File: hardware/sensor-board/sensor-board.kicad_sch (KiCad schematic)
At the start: 27 parts

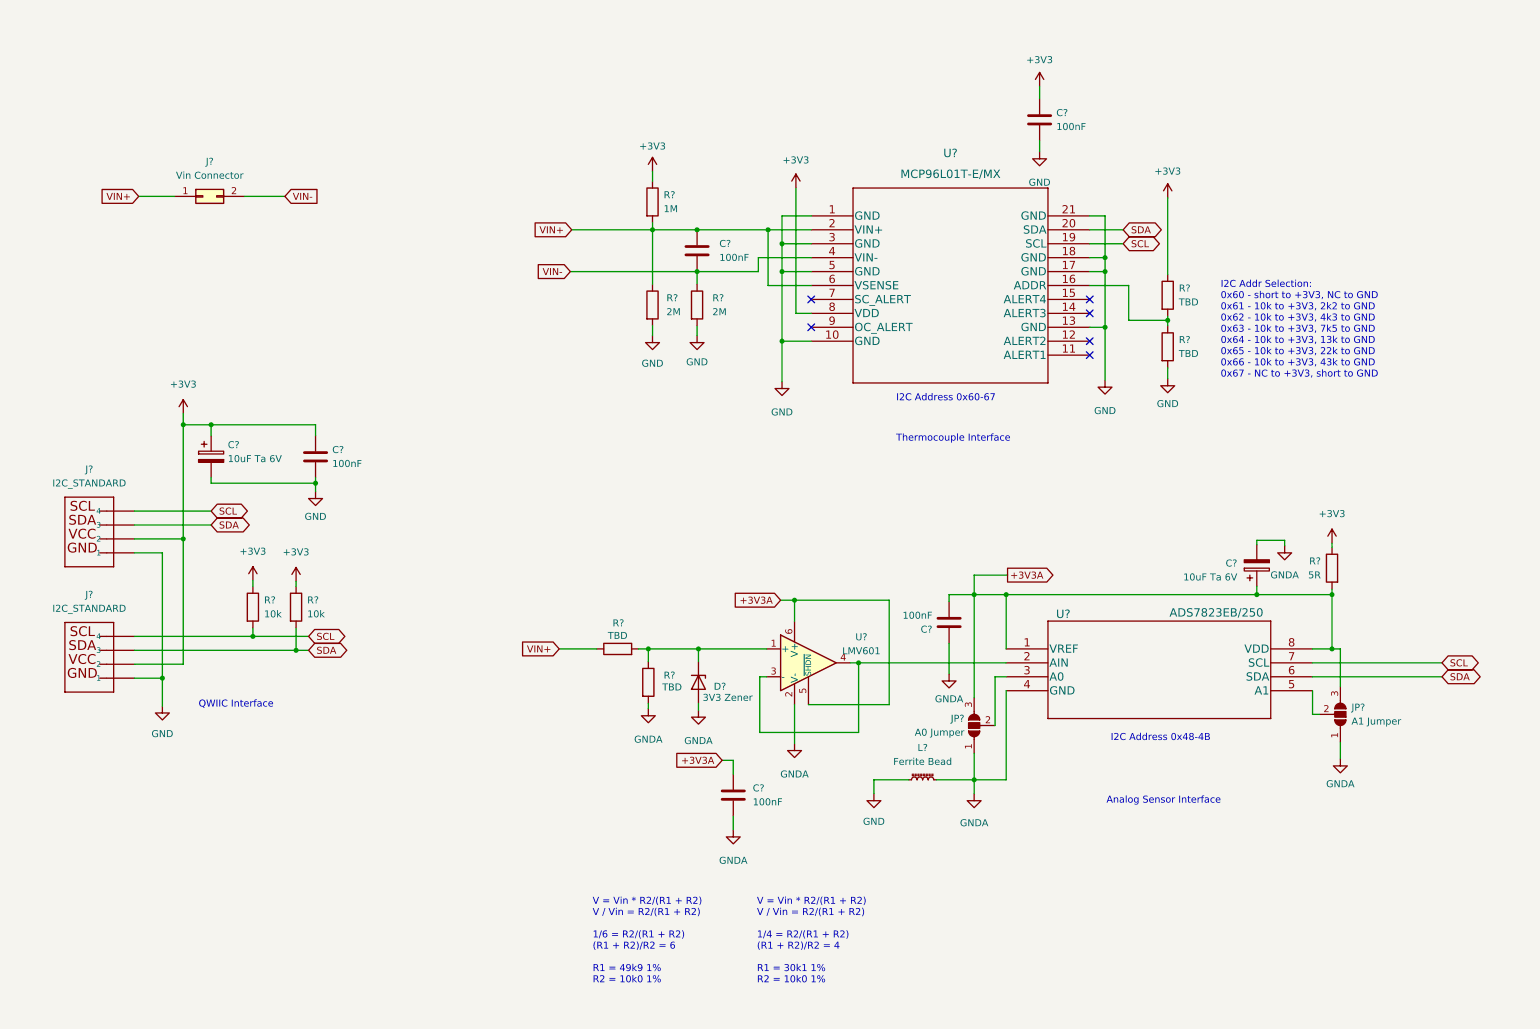
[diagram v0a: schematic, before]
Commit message: Added 1Wire sensor (over I2C) for outside temp
- coded up the first AnalogSourceBase and DS2482Source classes
- still need for ADC, thermocouple if... and internal temperature via
  internal ADC
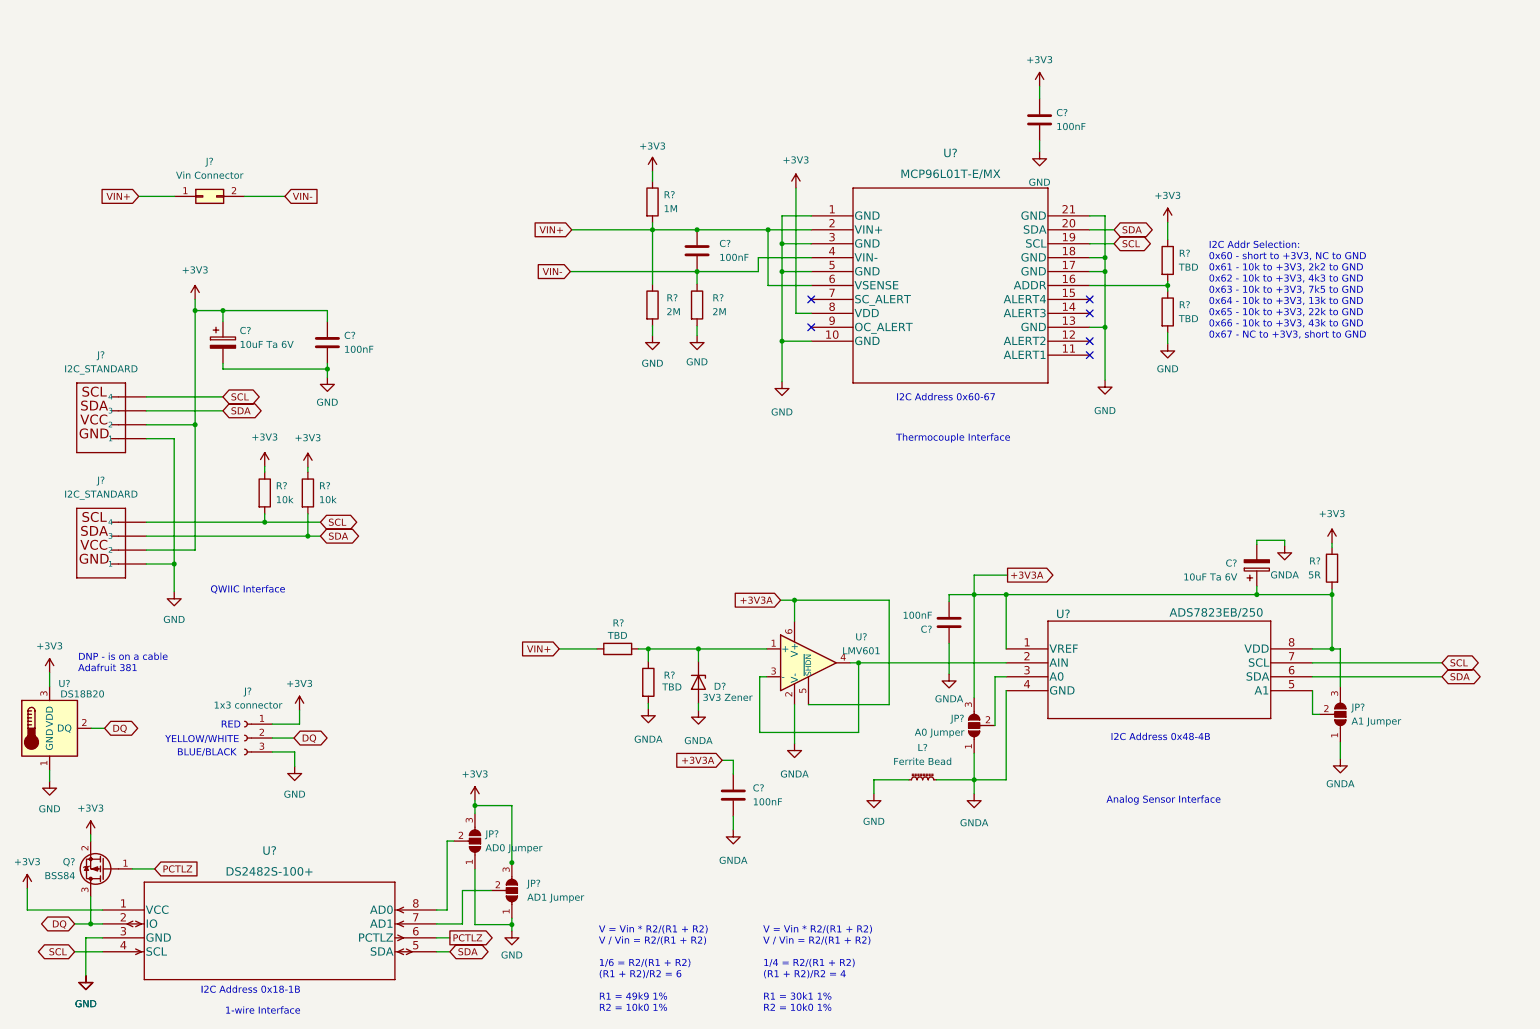
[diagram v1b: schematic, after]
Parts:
- added J?: 1x3 connector, symbol Connector:Conn_01x03_Female
- added JP?: AD1 Jumper, symbol Jumper:SolderJumper_3_Open
- added JP?: AD0 Jumper, symbol Jumper:SolderJumper_3_Open
- added Q?: BSS84, Package_TO_SOT_SMD:SOT-23, symbol Transistor_FET:BSS84
- added U?: DS18B20, Package_TO_SOT_THT:TO-92_Inline, symbol Sensor_Temperature:DS18B20
- added U?: DS2482S-100+, UltraLibrarian:ds2482s-100&plus_, symbol UltraLibrarian:DS2482S-100+
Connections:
- net +3V3: now also J?.1 (Pin_1), JP?.3 (B), JP?.3 (B), Q?.2 (S), U?.1 (VCC), U?.3 (VDD)
- net GND: now also J?.3 (Pin_3), JP?.1 (A), JP?.1 (A), U?.1 (GND), U?.3 (GND)
- net SCL: now also U?.4 (SCL)
- net SDA: now also U?.5 (SDA)
- new net: JP?.2 (C), U?.7 (AD1)
- new net: JP?.2 (C), U?.8 (AD0)
- new net DQ: J?.2 (Pin_2), Q?.3 (D), U?.2 (DQ), U?.2 (IO)
- new net PCTLZ: Q?.1 (G), U?.6 (PCTLZ)
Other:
- note added: "1-wire Interface"
- note added: "BLUE/BLACK"
- note added: "DNP - is on a cable Adafruit 381"
- note added: "I2C Address 0x18-1B"
- note added: "RED"
- note added: "YELLOW/WHITE"
- moved on the sheet: C?, J?, R?

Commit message: Layout v1 for sensors board
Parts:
- removed C? (x2): 10uF Ta 6V, symbol Device:C_Polarized
- added C1, C7: 10uF Ta 6V3, Capacitor_Tantalum_SMD:CP_EIA-3216-10_Kemet-I_Pad1.58x1.35mm_HandSolder, symbol Device:C_Polarized
- C2, C3, C4, C5, C6: renamed from C?; footprint (none) -> Capacitor_SMD:C_0805_2012Metric_Pad1.18x1.45mm_HandSolder
- D1: renamed from D?; value 3V3 Zener -> BZT52C3V3-7-F; footprint (none) -> Diode_SMD:D_SOD-123
- J1, J2: renamed from J?; value I2C_STANDARD -> QWIIC Connector; footprint UltraLibrarian:PRT-16766 -> Beirdo:QWIIC Connector
- J3: renamed from J?; footprint (none) -> TerminalBlock:TerminalBlock_Altech_AK300-2_P5.00mm
- J4: renamed from J?; footprint (none) -> TerminalBlock:TerminalBlock_Altech_AK300-3_P5.00mm
- JP1, JP2, JP3, JP4: renamed from JP?; footprint (none) -> Jumper:SolderJumper-3_P1.3mm_Open_Pad1.0x1.5mm
- L1: renamed from L?; footprint (none) -> Inductor_SMD:L_0805_2012Metric_Pad1.05x1.20mm_HandSolder
- R1, R10, R2, R3, R4, R5, R6, R7, R8, R9: renamed from R?; footprint (none) -> Resistor_SMD:R_0805_2012Metric_Pad1.20x1.40mm_HandSolder
- gave numbers to parts that had none: 6
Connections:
- net +3V3: now also C1.1
- net +3V3A: now also C5.1, JP3.3 (B), JP4.3 (B), R10.2, U5.1 (VREF), U5.8 (VDD), C7.1
- net GND: now also C1.2
- net GNDA: now also C7.2
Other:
- note added: "3.3V Zener"
- moved on the sheet: D1, R3, R4

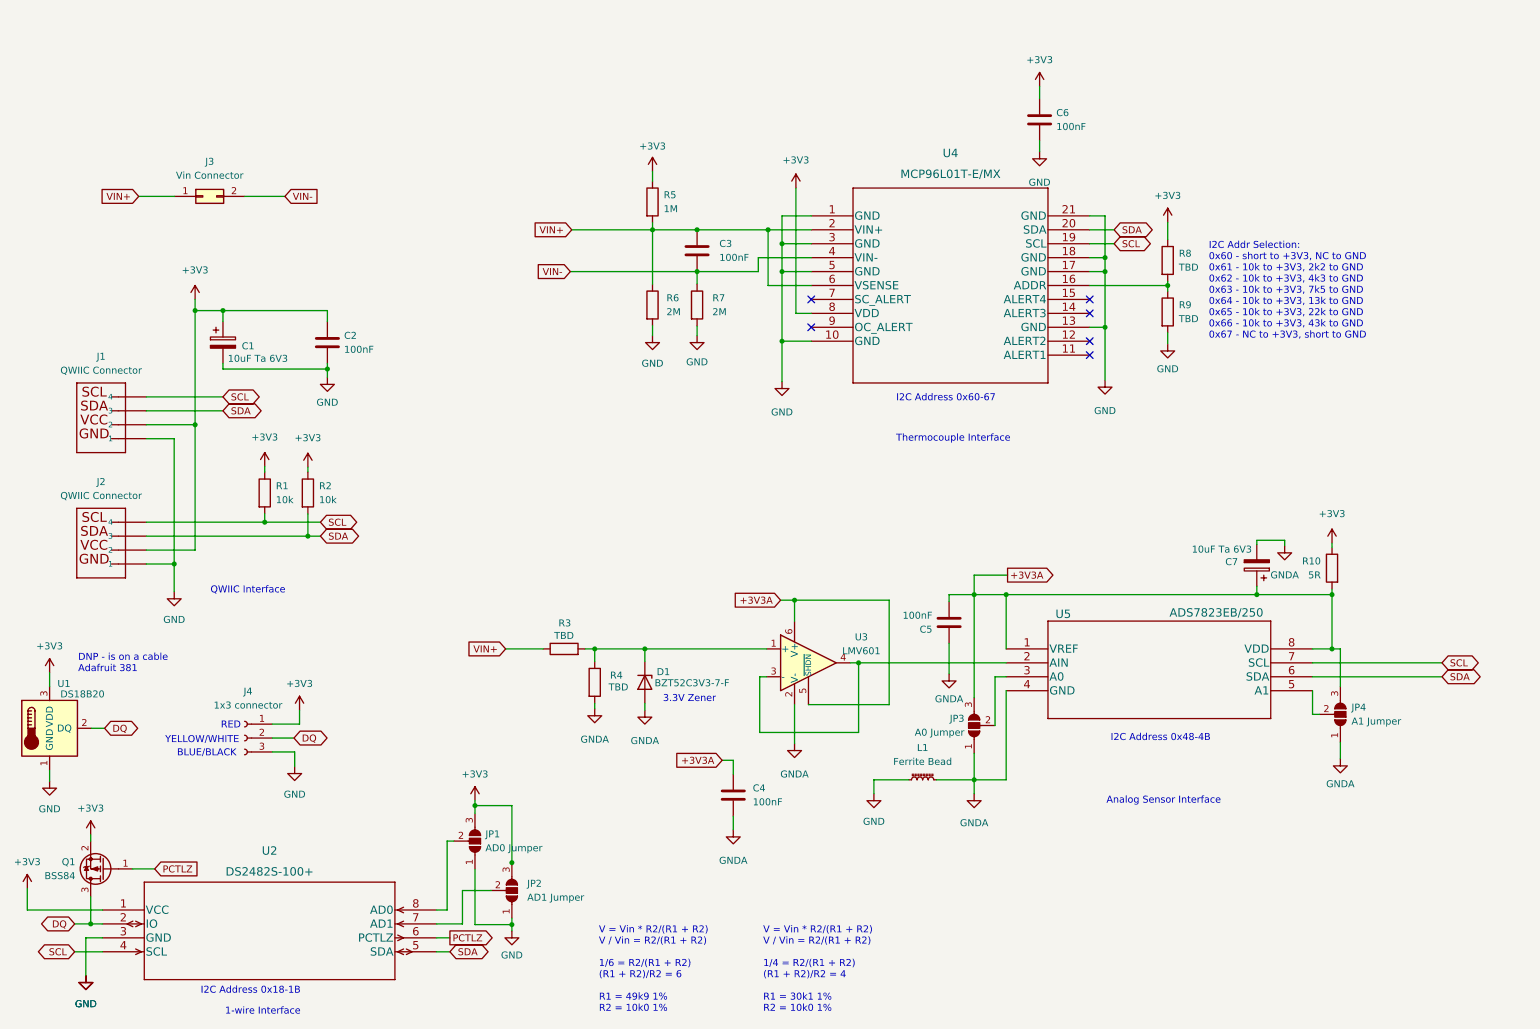
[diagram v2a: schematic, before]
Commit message: Added GPIO/EEPROM on sensor board
- this will allow me to connect the ignition wire, and also to have the
  boards report their capabilities to the firmware
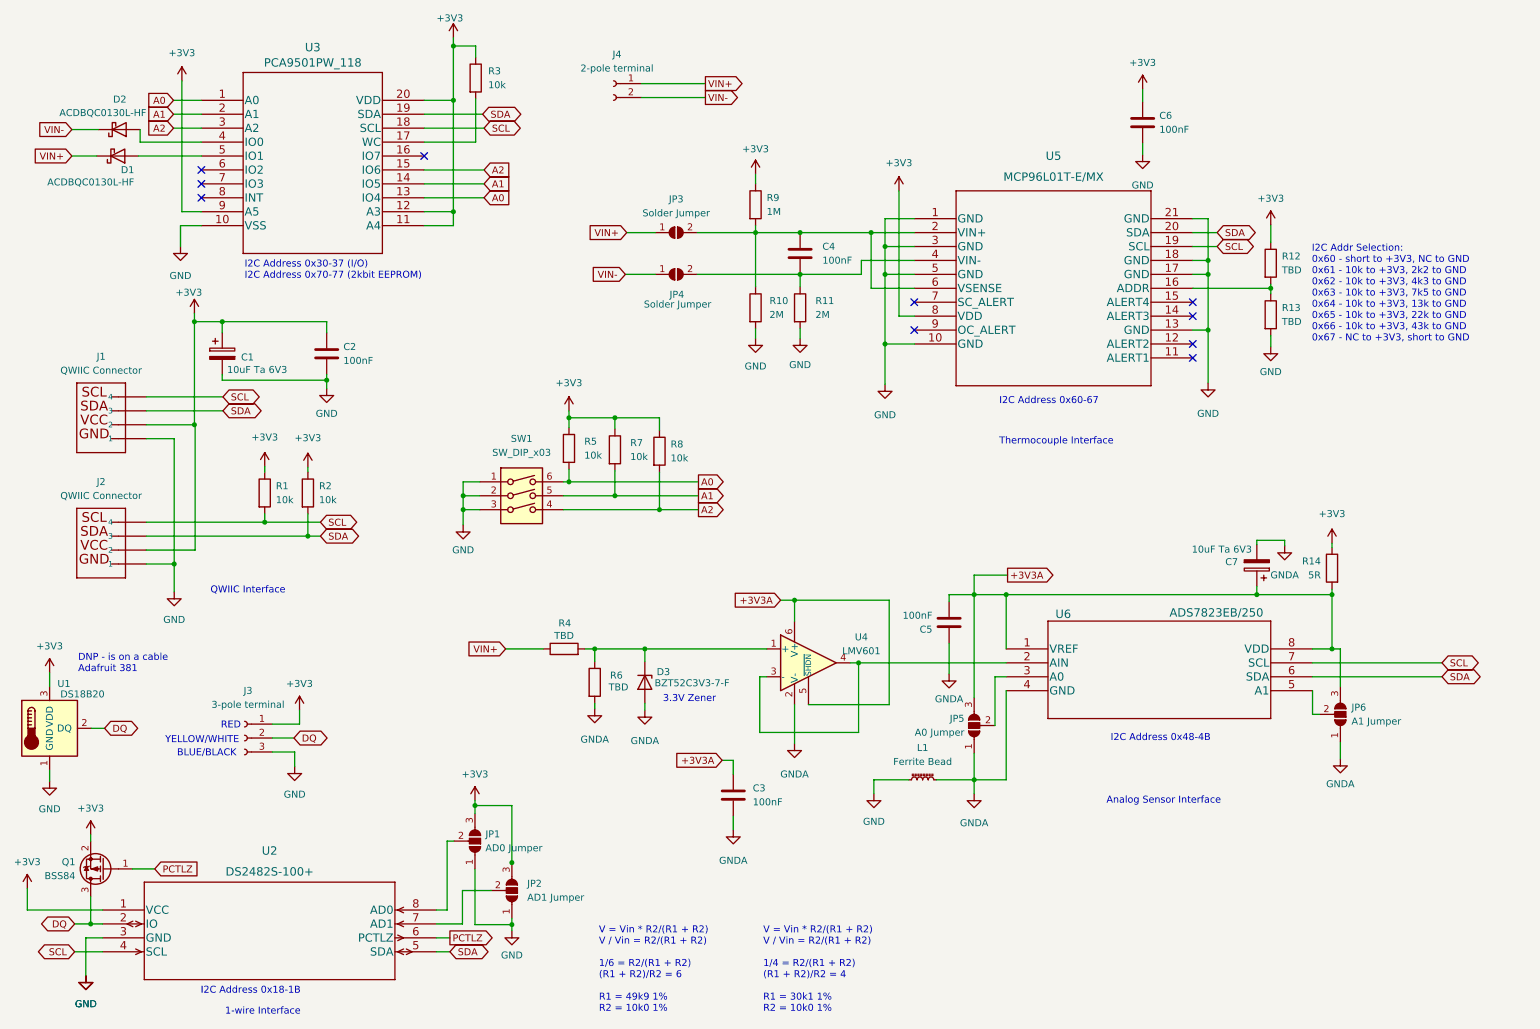
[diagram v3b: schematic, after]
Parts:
- removed J3: Vin Connector, TerminalBlock:TerminalBlock_Altech_AK300-2_P5.00mm, symbol Connector_Generic:Conn_02x01
- added D1, D2: ACDBQC0130L-HF, Diode_SMD:D_SOD-923, symbol Device:D_Schottky
- added J4: 2-pole terminal, TerminalBlock:TerminalBlock_Altech_AK300-2_P5.00mm, symbol Connector:Conn_01x02_Female
- added JP3, JP4: Solder Jumper, Jumper:SolderJumper-2_P1.3mm_Open_RoundedPad1.0x1.5mm, symbol Jumper:SolderJumper_2_Open
- added R3, R5, R7, R8: 10k, Resistor_SMD:R_0805_2012Metric_Pad1.20x1.40mm_HandSolder, symbol Device:R
- added SW1: SW_DIP_x03, Button_Switch_SMD:SW_DIP_SPSTx03_Slide_9.78x9.8mm_W8.61mm_P2.54mm, symbol Switch:SW_DIP_x03
- added U3: PCA9501PW_118, UltraLibrarian:PCA9501PW_118, symbol UltraLibrarian:PCA9501PW_118
- J3: renamed from J4; value 1x3 connector -> 3-pole terminal
- JP1, JP2: footprint Jumper:SolderJumper-3_P1.3mm_Open_Pad1.0x1.5mm -> Jumper:SolderJumper-3_P1.3mm_Open_RoundedPad1.0x1.5mm
- JP5: renamed from JP3; footprint Jumper:SolderJumper-3_P1.3mm_Open_Pad1.0x1.5mm -> Jumper:SolderJumper-3_P1.3mm_Open_RoundedPad1.0x1.5mm
- JP6: renamed from JP4; footprint Jumper:SolderJumper-3_P1.3mm_Open_Pad1.0x1.5mm -> Jumper:SolderJumper-3_P1.3mm_Open_RoundedPad1.0x1.5mm
- renumbered C4 to C3, C3 to C4, D1 to D3, R6 to R10, R7 to R11, R8 to R12, R9 to R13, R10 to R14, R3 to R4, R4 to R6, R5 to R9, U3 to U4, U4 to U5, U5 to U6
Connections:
- net +3V3: now also R3.1, R5.1, R7.1, R8.1, U3.11 (A4), U3.12 (A3), U3.20 (VDD), U3.9 (A5)
- net GND: now also SW1.1, SW1.2, SW1.3, U3.10 (VSS)
- net SCL: now also U3.18 (SCL)
- net SDA: now also U3.19 (SDA)
- net VIN+: now also D1.1 (K), J4.1 (Pin_1), JP3.1 (A); no longer C4.1, R10.1, R9.2, U5.2 (VIN+), U5.6 (VSENSE)
- net VIN-: now also D2.1 (K), J4.2 (Pin_2), JP4.1 (A); no longer C4.2, R11.1, U5.4 (VIN-)
- new net: C4.1, JP3.2 (B), R10.1, R9.2, U5.2 (VIN+), U5.6 (VSENSE)
- new net: D1.2 (A), U3.5 (IO1)
- new net: C4.2, JP4.2 (B), R11.1, U5.4 (VIN-)
- new net: D2.2 (A), U3.4 (IO0)
- new net: R3.2, U3.17 (WC)
- new net A0: R5.2, SW1.6, U3.1 (A0), U3.13 (IO4)
- new net A1: R7.2, SW1.5, U3.14 (IO5), U3.2 (A1)
- new net A2: R8.2, SW1.4, U3.15 (IO6), U3.3 (A2)
- no-connect marks 6 -> 10
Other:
- note added: "I2C Address 0x30-37 (I/O) I2C Address 0x70-77 (2kbit EEPROM)"
- moved on the sheet: C1, C2, C4, C6, R10, R11, R12, R13, R9, U5

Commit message: Added logging, added debug serial to mainboard
- also added eeprom read support, and the digital GPIO over I2C
- route the ignition wire as a digital GPIO so we can use it as an input
  to the state machine.
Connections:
- net at R3.2, U3.17 (WC): now also U3.16 (IO7)
- no-connect marks 10 -> 9
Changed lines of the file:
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@@
   (junction (at 130.81 102.87) (diameter 0) (color 0 0 0 0)
+  )
+  (junction (at 97.282 35.814) (diameter 0) (color 0 0 0 0)
   )
   (junction (at 230.886 57.404) (diameter 0) (color 0 0 0 0)
@@
   (no_connect (at 177.292 70.104))
   (no_connect (at 47.244 40.894))
-  (no_connect (at 87.884 38.354))
   (wire (pts (xy 118.999 128.27) (xy 118.999 130.556))
     (stroke (width 0) (type default) (color 0 0 0 0))
@@
     (stroke (width 0) (type default) (color 0 0 0 0))
   )
+  (wire (pts (xy 87.884 38.354) (xy 97.282 38.354))
+    (stroke (width 0) (type default) (color 0 0 0 0))
+  )
   (wire (pts (xy 26.162 180.975) (xy 29.21 180.975))
     (stroke (width 0) (type default) (color 0 0 0 0))
@@
     (stroke (width 0) (type default) (color 0 0 0 0))
   )
-  (wire (pts (xy 97.282 35.814) (xy 97.282 27.94))
+  (wire (pts (xy 97.282 27.94) (xy 97.282 35.814))
     (stroke (width 0) (type default) (color 0 0 0 0))
   )
@@
     (stroke (width 0) (type default) (color 0 0 0 0))
   )
+  (wire (pts (xy 97.282 35.814) (xy 97.282 38.354))
+    (stroke (width 0) (type default) (color 0 0 0 0))
+  )
